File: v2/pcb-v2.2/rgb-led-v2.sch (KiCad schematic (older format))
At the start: 11 parts, among them CON1 BARREL_JACK, SW1 SPST

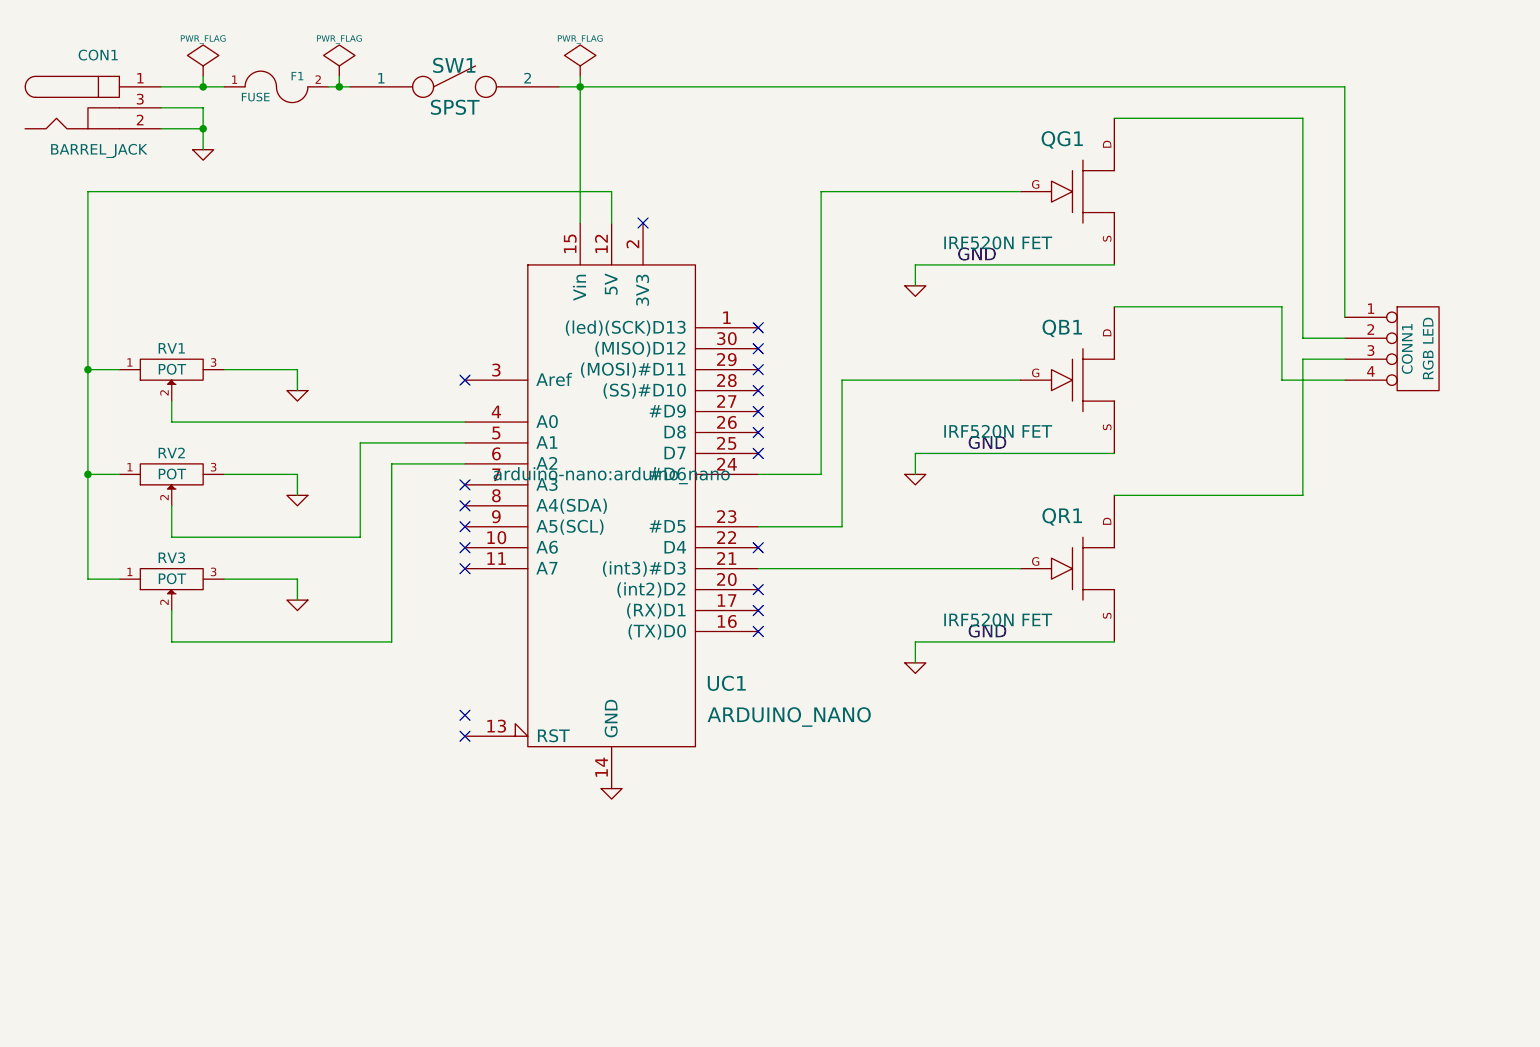
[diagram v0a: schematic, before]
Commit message: Add pin headers to schema
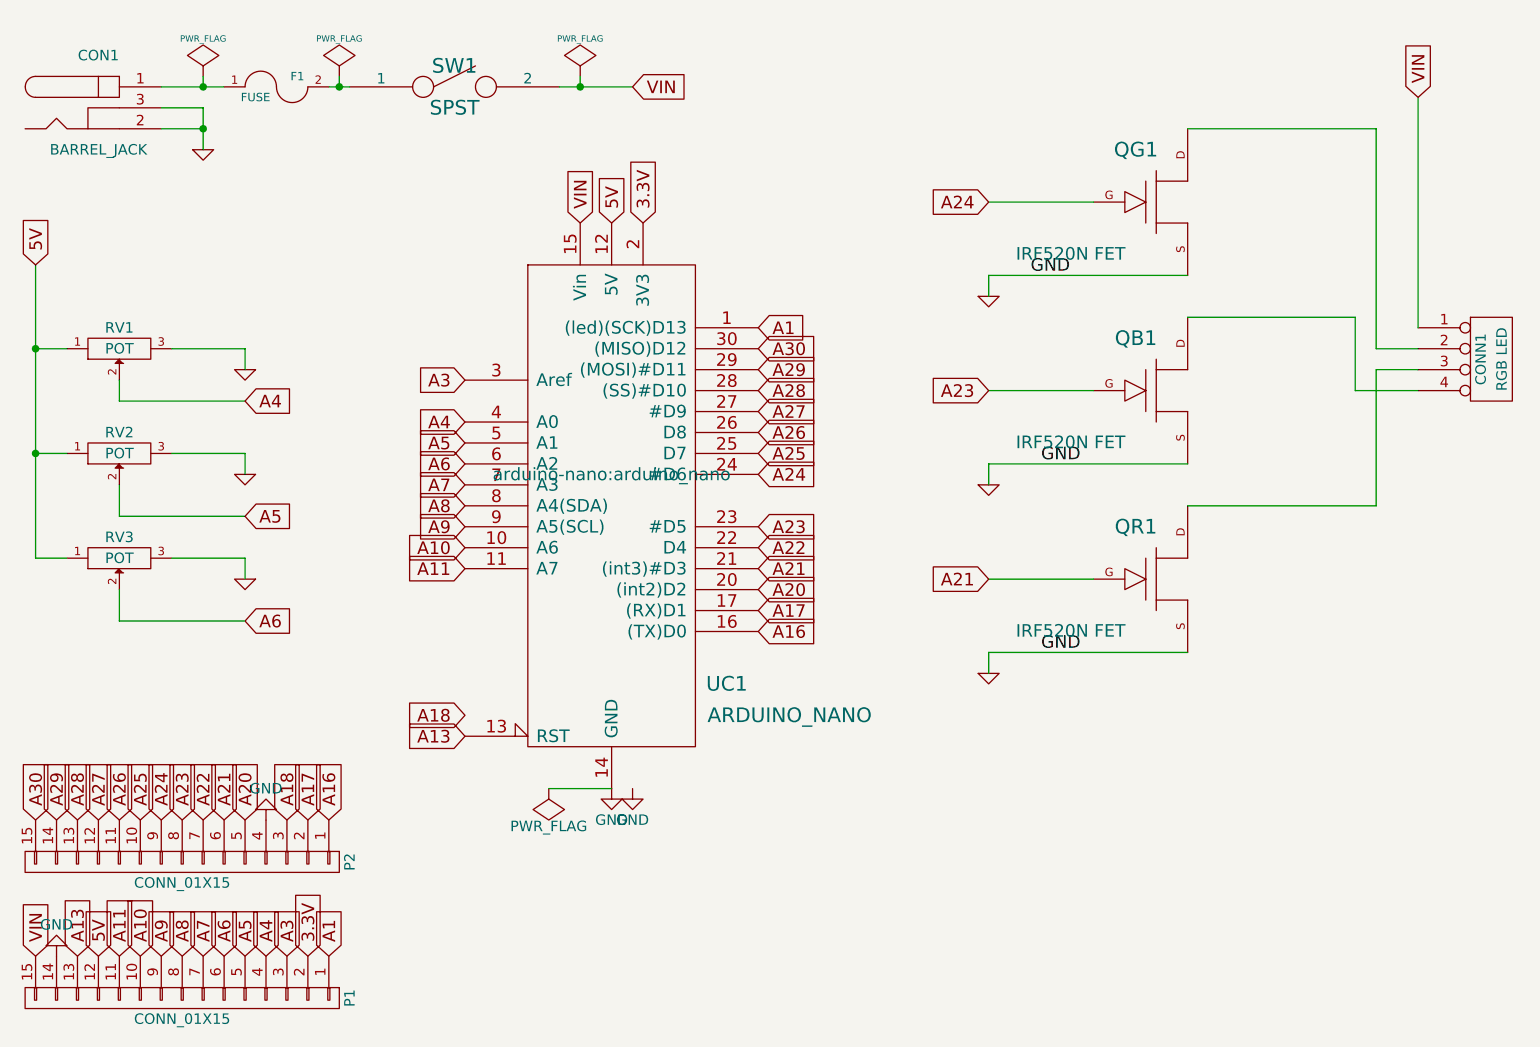
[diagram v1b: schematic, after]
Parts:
- added P1, P2: CONN_01X15, Pin_Headers:Pin_Header_Straight_1x15_Pitch2.54mm, symbol CONN_01X15
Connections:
- net GND: now also P1.14 (P14), P2.4 (P4)
- net A21: now reaches QR1.G, UC1.21 ((int3)#D3)
- net A21: now also P2.6 (P6)
- net A24: now reaches QG1.G, UC1.24 (#D6)
- net A24: now also P2.9 (P9)
- net A23: now reaches QB1.G, UC1.23 (#D5)
- net A23: now also P2.8 (P8)
- net VIN: now reaches CONN1.1 (P1), SW1.2, UC1.15 (Vin)
- net VIN: now also P1.15 (P15)
- net 5V: now reaches RV1.1, RV2.1, RV3.1, UC1.12 (5V)
- net 5V: now also P1.12 (P12)
- net A4: now reaches RV1.2, UC1.4 (A0)
- net A4: now also P1.4 (P4)
- net A5: now reaches RV2.2, UC1.5 (A1)
- net A5: now also P1.5 (P5)
- net A6: now reaches RV3.2, UC1.6 (A2)
- net A6: now also P1.6 (P6)
- net A1: now reaches UC1.1 ((led)(SCK)D13)
- net A1: now also P1.1 (P1)
- net A10: now reaches UC1.10 (A6)
- net A10: now also P1.10 (P10)
- net A11: now reaches UC1.11 (A7)
- net A11: now also P1.11 (P11)
- net A13: now reaches UC1.13 (RST)
- net A13: now also P1.13 (P13)
- net A16: now reaches UC1.16 ((TX)D0)
- net A16: now also P2.1 (P1)
- net A17: now reaches UC1.17 ((RX)D1)
- net A17: now also P2.2 (P2)
- net A18: now reaches UC1.18 (RST)
- net A18: now also P2.3 (P3)
- net 3.3V: now reaches UC1.2 (3V3)
- net 3.3V: now also P1.2 (P2)
- net A20: now reaches UC1.20 ((int2)D2)
- net A20: now also P2.5 (P5)
- net A22: now reaches UC1.22 (D4)
- net A22: now also P2.7 (P7)
- net A25: now reaches UC1.25 (D7)
- net A25: now also P2.10 (P10)
- net A26: now reaches UC1.26 (D8)
- net A26: now also P2.11 (P11)
- net A27: now reaches UC1.27 (#D9)
- net A27: now also P2.12 (P12)
- net A28: now reaches UC1.28 ((SS)#D10)
- net A28: now also P2.13 (P13)
- net A29: now reaches UC1.29 ((MOSI)#D11)
- net A29: now also P2.14 (P14)
- net A3: now reaches UC1.3 (Aref)
- net A3: now also P1.3 (P3)
- net A30: now reaches UC1.30 ((MISO)D12)
- net A30: now also P2.15 (P15)
- net A7: now reaches UC1.7 (A3)
- net A7: now also P1.7 (P7)
- net A8: now reaches UC1.8 (A4(SDA))
- net A8: now also P1.8 (P8)
- net A9: now reaches UC1.9 (A5(SCL))
- net A9: now also P1.9 (P9)
- no-connect marks 20 -> 0
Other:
- moved on the sheet: CONN1, QB1, QG1, QR1, RV1, RV2, RV3

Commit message: Two push buttons (fixes #2)
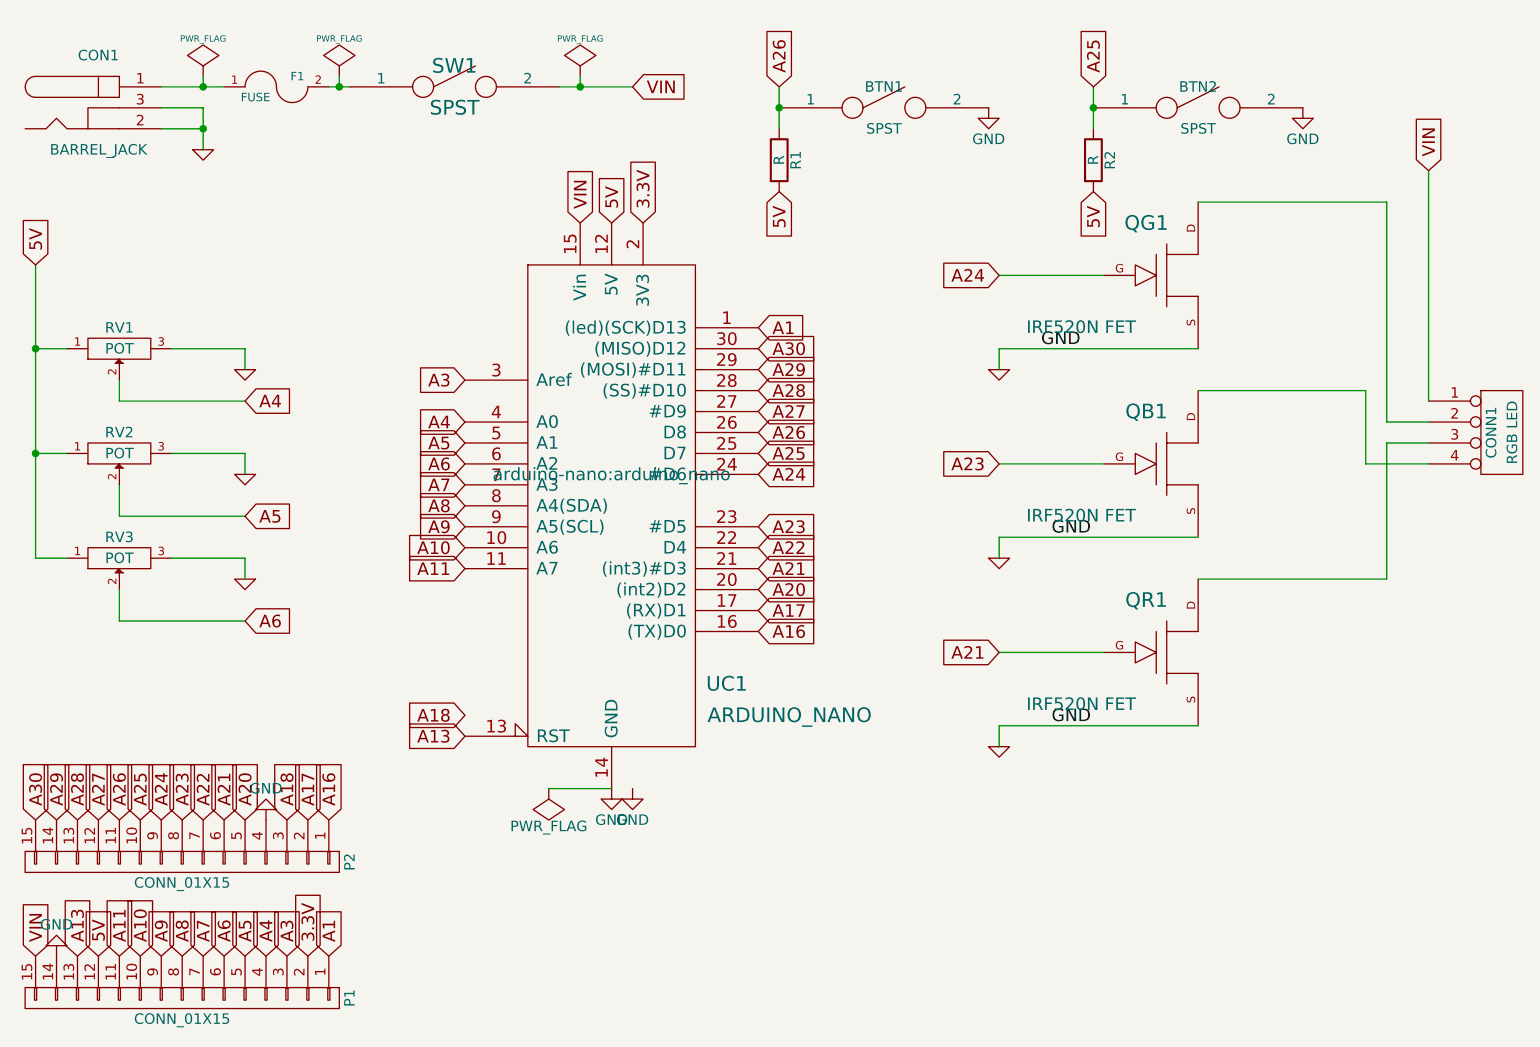
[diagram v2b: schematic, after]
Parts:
- added BTN1, BTN2: SPST, rgbled-custom:PUSHBUTTON_TS044S, symbol SPST
- added R1, R2: R, Resistors_THT:R_Axial_DIN0207_L6.3mm_D2.5mm_P10.16mm_Horizontal, symbol R
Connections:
- net 5V: now also R1.2, R2.2
- net A25: now also BTN2.1, R2.1
- net A26: now also BTN1.1, R1.1
- net GND: now also BTN1.2, BTN2.2
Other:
- moved on the sheet: CONN1, QB1, QG1, QR1
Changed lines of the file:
@@
 L FET_N QR1
 U 1 1 5476D26F
-P 6000 3200
-F 0 "QR1" H 5903 3450 70  0000 C CNN
-F 1 "IRF520N FET" H 5853 2953 60  0000 R CNN
-F 2 "library:IRF520N" H 6000 3200 60  0001 C CNN
-F 3 "~" H 6000 3200 60  0000 C CNN
-	1    6000 3200
+P 6050 3550
+F 0 "QR1" H 5953 3800 70  0000 C CNN
+F 1 "IRF520N FET" H 5903 3303 60  0000 R CNN
+F 2 "library:IRF520N" H 6050 3550 60  0001 C CNN
+F 3 "~" H 6050 3550 60  0000 C CNN
+	1    6050 3550
 	1    0    0    -1
 $EndComp
@@
 L FET_N QG1
 U 1 1 5476D286
-P 6000 1400
-F 0 "QG1" H 5903 1650 70  0000 C CNN
-F 1 "IRF520N FET" H 5853 1153 60  0000 R CNN
-F 2 "library:IRF520N" H 6000 1400 60  0001 C CNN
-F 3 "~" H 6000 1400 60  0000 C CNN
-	1    6000 1400
+P 6050 1750
+F 0 "QG1" H 5953 2000 70  0000 C CNN
+F 1 "IRF520N FET" H 5903 1503 60  0000 R CNN
+F 2 "library:IRF520N" H 6050 1750 60  0001 C CNN
+F 3 "~" H 6050 1750 60  0000 C CNN
+	1    6050 1750
 	1    0    0    -1
 $EndComp
@@
 L FET_N QB1
 U 1 1 5476D28C
-P 6000 2300
-F 0 "QB1" H 5903 2550 70  0000 C CNN
-F 1 "IRF520N FET" H 5853 2053 60  0000 R CNN
-F 2 "library:IRF520N" H 6000 2300 60  0001 C CNN
-F 3 "~" H 6000 2300 60  0000 C CNN
-	1    6000 2300
+P 6050 2650
+F 0 "QB1" H 5953 2900 70  0000 C CNN
+F 1 "IRF520N FET" H 5903 2403 60  0000 R CNN
+F 2 "library:IRF520N" H 6050 2650 60  0001 C CNN
+F 3 "~" H 6050 2650 60  0000 C CNN
+	1    6050 2650
 	1    0    0    -1
 $EndComp
@@
 L CONN_4 CONN1
 U 1 1 5476D68C
-P 7600 2150
-F 0 "CONN1" V 7550 2150 50  0000 C CNN
-F 1 "RGB LED" V 7650 2150 50  0000 C CNN
-F 2 "library:PIN_ARRAY_4x1_THICK" H 7600 2150 60  0001 C CNN
-F 3 "~" H 7600 2150 60  0000 C CNN
-	1    7600 2150
+P 7650 2500
+F 0 "CONN1" V 7600 2500 50  0000 C CNN
+F 1 "RGB LED" V 7700 2500 50  0000 C CNN
+F 2 "library:PIN_ARRAY_4x1_THICK" H 7650 2500 60  0001 C CNN
+F 3 "~" H 7650 2500 60  0000 C CNN
+	1    7650 2500
 	1    0    0    -1
 $EndComp
@@
 $EndComp
 $Comp
-L arduino_nano UC1
-U 1 1 54776301
-P 3400 2650
-F 0 "UC1" H 3950 1600 70  0000 C CNN
-F 1 "ARDUINO_NANO" H 4250 1450 70  0000 C CNN
-F 2 "arduino-nano:arduino_nano" H 3400 2600 60  0000 C CNN
-F 3 "" H 3400 2650 60  0000 C CNN
-	1    3400 2650
-	1    0    0    -1
-$EndComp
-$Comp
 L GND-RESCUE-rgb-led-v2 #PWR01
 U 1 1 5477A4E7
-P 5200 1850
-F 0 "#PWR01" H 5200 1850 30  0001 C CNN
-F 1 "GND" H 5200 1780 30  0001 C CNN
-F 2 "" H 5200 1850 60  0000 C CNN
-F 3 "" H 5200 1850 60  0000 C CNN
-	1    5200 1850
+P 5250 2200
+F 0 "#PWR01" H 5250 2200 30  0001 C CNN
+F 1 "GND" H 5250 2130 30  0001 C CNN
+F 2 "" H 5250 2200 60  0000 C CNN
+F 3 "" H 5250 2200 60  0000 C CNN
+	1    5250 2200
 	1    0    0    -1
 $EndComp
@@
 L GND-RESCUE-rgb-led-v2 #PWR02
 U 1 1 5477A4F4
-P 5200 2750
-F 0 "#PWR02" H 5200 2750 30  0001 C CNN
-F 1 "GND" H 5200 2680 30  0001 C CNN
-F 2 "" H 5200 2750 60  0000 C CNN
-F 3 "" H 5200 2750 60  0000 C CNN
-	1    5200 2750
+P 5250 3100
+F 0 "#PWR02" H 5250 3100 30  0001 C CNN
+F 1 "GND" H 5250 3030 30  0001 C CNN
+F 2 "" H 5250 3100 60  0000 C CNN
+F 3 "" H 5250 3100 60  0000 C CNN
+	1    5250 3100
 	1    0    0    -1
 $EndComp
@@
 L GND-RESCUE-rgb-led-v2 #PWR09
 U 1 1 5477A4FA
-P 5200 3650
-F 0 "#PWR09" H 5200 3650 30  0001 C CNN
-F 1 "GND" H 5200 3580 30  0001 C CNN
-F 2 "" H 5200 3650 60  0000 C CNN
-F 3 "" H 5200 3650 60  0000 C CNN
-	1    5200 3650
-	1    0    0    -1
-$EndComp
-Text Label 5450 3550 0    60   ~ 0
+P 5250 4000
+F 0 "#PWR09" H 5250 4000 30  0001 C CNN
+F 1 "GND" H 5250 3930 30  0001 C CNN
+F 2 "" H 5250 4000 60  0000 C CNN
+F 3 "" H 5250 4000 60  0000 C CNN
+	1    5250 4000
+	1    0    0    -1
+$EndComp
+Text Label 5500 3900 0    60   ~ 0
 GND
-Text Label 5400 1750 0    60   ~ 0
+Text Label 5450 2100 0    60   ~ 0
 GND
-Text Label 5450 2650 0    60   ~ 0
+Text Label 5500 3000 0    60   ~ 0
 GND
 $Comp
@@
 Text GLabel 4100 2950 2    60   Input ~ 0
 A23
-Text GLabel 5200 2300 0    60   Input ~ 0
+Text GLabel 5250 2650 0    60   Input ~ 0
 A23
 Text GLabel 4100 2700 2    60   Input ~ 0
 A24
-Text GLabel 5200 1400 0    60   Input ~ 0
+Text GLabel 5250 1750 0    60   Input ~ 0
 A24
 Wire Wire Line
-	5700 3200 5200 3200
+	5750 3550 5250 3550
 Wire Wire Line
 	3250 800  3250 850
@@
 	2050 850  2150 850
 Wire Wire Line
-	6150 3550 5200 3550
-Wire Wire Line
-	5200 3550 5200 3650
+	6200 3900 5250 3900
+Wire Wire Line
+	5250 3900 5250 4000
 Wire Wire Line
 	1450 950  1450 1150
@@
 	1250 850  1550 850
 Wire Wire Line
-	5200 2650 5200 2750
-Wire Wire Line
-	5200 1750 5200 1850
-Wire Wire Line
-	7250 900  7250 2000
-Wire Wire Line
-	6950 1950 6150 1950
-Wire Wire Line
-	6950 2300 6950 1950
-Wire Wire Line
-	7250 2300 6950 2300
-Wire Wire Line
-	7050 2850 6150 2850
-Wire Wire Line
-	7050 2200 7050 2850
-Wire Wire Line
-	7250 2200 7050 2200
-Wire Wire Line
-	7050 1050 6150 1050
-Wire Wire Line
-	7050 2100 7050 1050
-Wire Wire Line
-	7250 2100 7050 2100
-Wire Wire Line
-	6150 2650 5200 2650
-Wire Wire Line
-	6150 1750 5200 1750
-Wire Wire Line
-	5200 1400 5700 1400
-Wire Wire Line
-	5200 2300 5700 2300
+	5250 3000 5250 3100
+Wire Wire Line
+	5250 2100 5250 2200
+Wire Wire Line
+	7300 1250 7300 2350
+Wire Wire Line
+	7000 2300 6200 2300
+Wire Wire Line
+	7000 2650 7000 2300
+Wire Wire Line
+	7300 2650 7000 2650
+Wire Wire Line
+	7100 3200 6200 3200
+Wire Wire Line
+	7100 2550 7100 3200
+Wire Wire Line
+	7300 2550 7100 2550
+Wire Wire Line
+	7100 1400 6200 1400
+Wire Wire Line
+	7100 2450 7100 1400
+Wire Wire Line
+	7300 2450 7100 2450
+Wire Wire Line
+	6200 3000 5250 3000
+Wire Wire Line
+	6200 2100 5250 2100
+Wire Wire Line
+	5250 1750 5750 1750
+Wire Wire Line
+	5250 2650 5750 2650
 Wire Wire Line
 	1050 2750 1050 2900
@@
 Wire Wire Line
 	650  1700 650  3100
-Text GLabel 5200 3200 0    60   Input ~ 0
+Text GLabel 5250 3550 0    60   Input ~ 0
 A21
 Text GLabel 4100 3150 2    60   Input ~ 0
@@
 Wire Wire Line
 	3150 850  3500 850
-Text GLabel 7250 900  1    60   Input ~ 0
+Text GLabel 7300 1250 1    60   Input ~ 0
 VIN
 Wire Wire Line
@@
 Wire Wire Line
 	3100 4200 3400 4200
+$Comp
+L SPST BTN2
+U 1 1 58AA2DA7
+P 6200 950
+F 0 "BTN2" H 6200 1050 50  0000 C CNN
+F 1 "SPST" H 6200 850 50  0000 C CNN
+F 2 "rgbled-custom:PUSHBUTTON_TS044S" H 6200 950 50  0001 C CNN
+F 3 "" H 6200 950 50  0000 C CNN
+	1    6200 950
+	1    0    0    -1
+$EndComp
+$Comp
+L SPST BTN1
+U 1 1 58AA2EE6
+P 4700 950
+F 0 "BTN1" H 4700 1050 50  0000 C CNN
+F 1 "SPST" H 4700 850 50  0000 C CNN
+F 2 "rgbled-custom:PUSHBUTTON_TS044S" H 4700 950 50  0001 C CNN
+F 3 "" H 4700 950 50  0000 C CNN
+	1    4700 950
+	1    0    0    -1
+$EndComp
+$Comp
+L arduino_nano UC1
+U 1 1 54776301
+P 3400 2650
+F 0 "UC1" H 3950 1600 70  0000 C CNN
+F 1 "ARDUINO_NANO" H 4250 1450 70  0000 C CNN
+F 2 "arduino-nano:arduino_nano" H 3400 2600 60  0000 C CNN
+F 3 "" H 3400 2650 60  0000 C CNN
+	1    3400 2650
+	1    0    0    -1
+$EndComp
+$Comp
+L GND #PWR016
+U 1 1 58AA36FE
+P 5200 950
+F 0 "#PWR016" H 5200 700 50  0001 C CNN
+F 1 "GND" H 5200 800 50  0000 C CNN
+F 2 "" H 5200 950 50  0000 C CNN
+F 3 "" H 5200 950 50  0000 C CNN
+	1    5200 950
+	1    0    0    -1
+$EndComp
+$Comp
+L GND #PWR017
+U 1 1 58AA373F
+P 6700 950
+F 0 "#PWR017" H 6700 700 50  0001 C CNN
+F 1 "GND" H 6700 800 50  0000 C CNN
+F 2 "" H 6700 950 50  0000 C CNN
+F 3 "" H 6700 950 50  0000 C CNN
+	1    6700 950
+	1    0    0    -1
+$EndComp
+$Comp
+L R R2
+U 1 1 58AA38B0
+P 5700 1200
+F 0 "R2" V 5780 1200 50  0000 C CNN
+F 1 "R" V 5700 1200 50  0000 C CNN
+F 2 "Resistors_THT:R_Axial_DIN0207_L6.3mm_D2.5mm_P10.16mm_Horizontal" V 5630 1200 50  0001 C CNN
+F 3 "" H 5700 1200 50  0000 C CNN
+	1    5700 1200
+	1    0    0    -1
+$EndComp
+$Comp
+L R R1
+U 1 1 58AA3913
+P 4200 1200
+F 0 "R1" V 4280 1200 50  0000 C CNN
+F 1 "R" V 4200 1200 50  0000 C CNN
+F 2 "Resistors_THT:R_Axial_DIN0207_L6.3mm_D2.5mm_P10.16mm_Horizontal" V 4130 1200 50  0001 C CNN
+F 3 "" H 4200 1200 50  0000 C CNN
+	1    4200 1200
+	1    0    0    -1
+$EndComp
+Wire Wire Line
+	4200 850  4200 1050
+Wire Wire Line
+	5700 850  5700 1050
+Connection ~ 5700 950
+Connection ~ 4200 950
+Text GLabel 4200 850  1    60   Input ~ 0
+A26
+Text GLabel 5700 850  1    60   Input ~ 0
+A25
+Text GLabel 4200 1350 3    60   Input ~ 0
+5V
+Text GLabel 5700 1350 3    60   Input ~ 0
+5V
 $EndSCHEMATC
